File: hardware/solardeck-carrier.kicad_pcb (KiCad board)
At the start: 6 copper layers, 222 x 160 mm, 34 parts, among them J1 DF40C-100DS-0.4V, J2 DF40C-100DS-0.4V, SW1 JS102011SAQN, U1 BQ25895RTWR, U10 W25Q128JVS, U11 DS3231MZ+, U14 TMUX1575YCJR, U15 SN74LVC1G08DBVR, U16 VL805-Q6, U18 ST4SIM-200M, U19 TPS22918DBVR, U2 TPS62840DLYR, U20 INA3221AIRGVR, U21 BQ27441-G1A, U22 TPS2051BDBVR, U23 BMA400, U24 BMP390, U25 TMP112AIDRLR, U26 TUSB320RWBR, U27 TXU0104PWR, U28 MAX98357A, U3 TPS61088RHLR, U4 TPS63020DSJR, U5 BQ25504RGTR, U8 RP2350B, U9 APS6404L-3SQR-SN

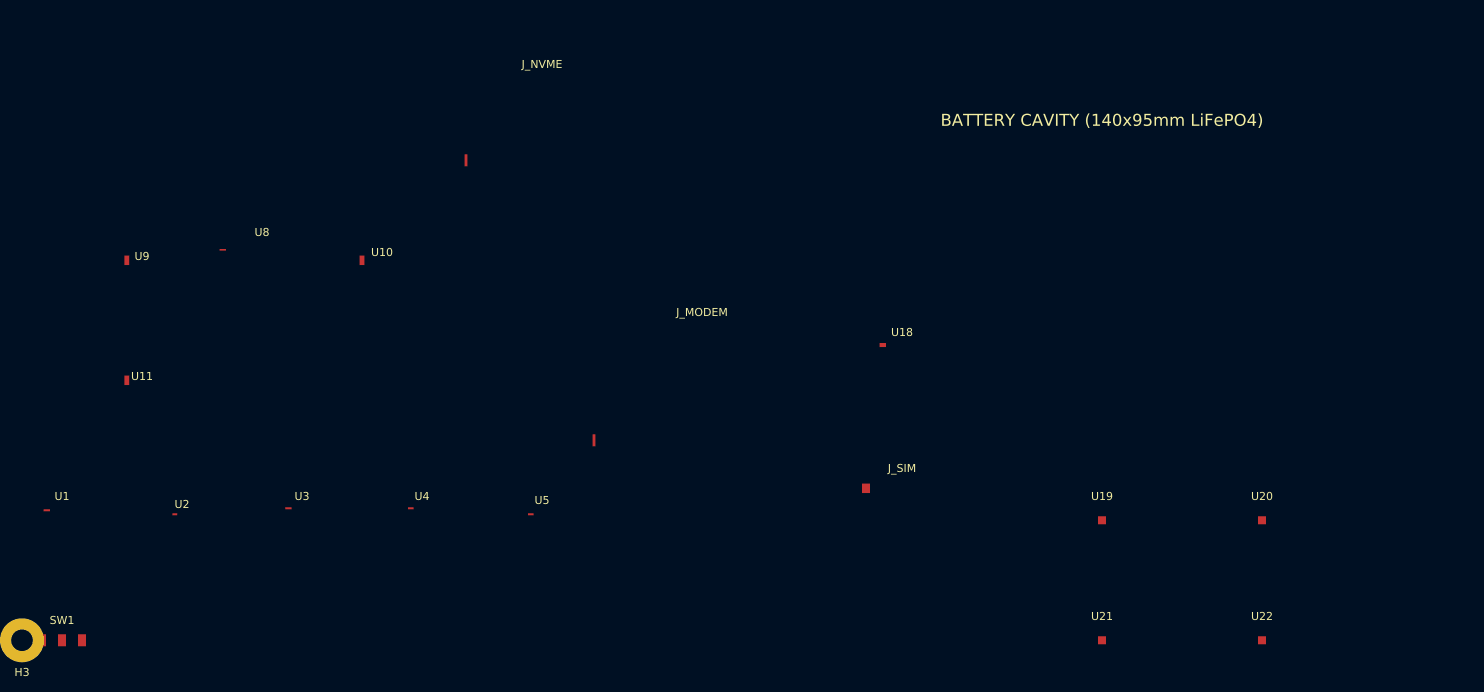
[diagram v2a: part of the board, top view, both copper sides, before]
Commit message: schematic: capture 10 more BOM line items (30/62 -> 40/62) with real LCSC numbers
Batch 2: STUSB4500QTR (PD sink), BQ29700DSET (battery PCM), LM66100DCKR (VBUS
OR-ing), PN5321A3HN (NFC + crypto signer), TPD4E05U06 (ESD TVS), dual
SPH0645LM4H-B (MEMS beamforming pair at 65mm), E22-900M22S (LoRa), PCM5102APWR
(headphone DAC), DRV2605LDGST (haptic).

Footprints datasheet-anchored, incl. corrections the searches caught (TPD4E05
is USON-10 not SOT-23-6, LM66100 is SC-70-6, PCM5102A is TSSOP-20, DRV2605L is
VSSOP-10). capture_schematic_parts.py now also emits kicad_pcb footprint blocks
(reference-grade single pad per U5/U14 convention) and is fully idempotent.
Phase 11 guard extended: live prose restatements must match the netlist.

spec_values baseline 30 -> 40; README/HANDOFF prose normalized; STATUS regenerated.

Co-Authored-By: DeepSeek V4-Flash 0731 <noreply@anthropic.com>
Harness: pi (openrouter/deepseek/deepseek-v4-flash-0731, session 01a15a7c)
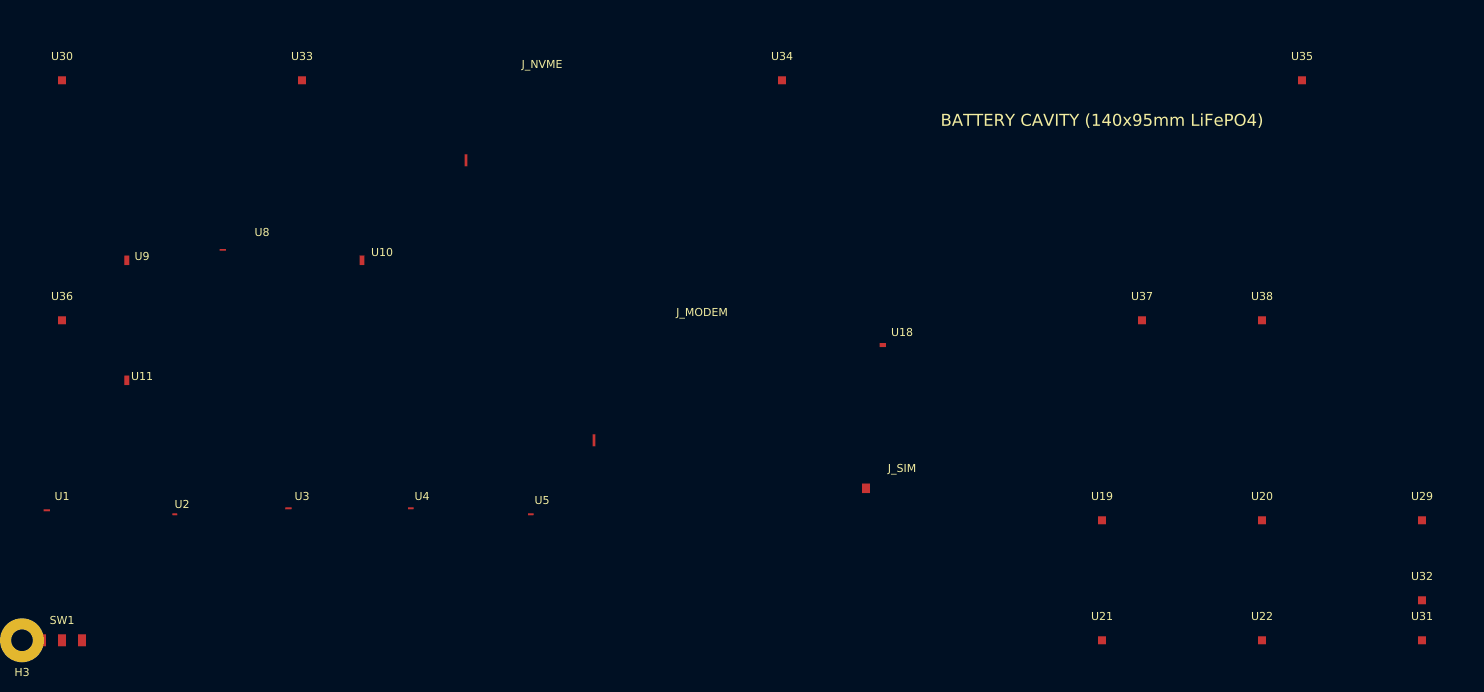
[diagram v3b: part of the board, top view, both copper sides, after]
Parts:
- added U29: STUSB4500QTR, Package_DFN_QFN:VQFN-24-1EP_4x4mm_P0.5mm, F.Cu at (190.0, 135.0)
- added U30: PN5321A3HN, Package_DFN_QFN:HVQFN-40_6x6mm_P0.5mm, F.Cu at (20.0, 80.0)
- added U31: BQ29700DSET, Package_DFN_QFN:WSON-6_1.5x1.5mm_P0.5mm, F.Cu at (190.0, 150.0)
- added U32: LM66100DCKR, Package_TO_SOT_SMD:SC-70-6, F.Cu at (190.0, 145.0)
- added U33: TPD4E05U06, Package_DFN_QFN:USON-10_2.5x1mm_P0.5mm, F.Cu at (50.0, 80.0)
- added U34: SPH0645LM4H-B, Package_LGA:MIC-SMD-6P_3.5x2.65mm_P0.9mm, F.Cu at (110.0, 80.0)
- added U35: SPH0645LM4H-B, Package_LGA:MIC-SMD-6P_3.5x2.65mm_P0.9mm, F.Cu at (175.0, 80.0)
- added U36: E22-900M22S, Module_EByte:E22-900M22S_20x14mm, F.Cu at (20.0, 110.0)
- added U37: PCM5102APWR, Package_SO:TSSOP-20_6.5x4.4mm_P0.65mm, F.Cu at (155.0, 110.0)
- added U38: DRV2605LDGST, Package_TO_SOT_SMD:VSSOP-10_3x4.9mm_P0.5mm, F.Cu at (170.0, 110.0)
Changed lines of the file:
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@@
     (pad "1" smd rect (at 0 0) (size 1.0 1.0) (layers "F.Cu" "F.Paste" "F.Mask"))
   )
-)
+  (footprint "Package_DFN_QFN:VQFN-24-1EP_4x4mm_P0.5mm" (layer "F.Cu")
+    (at 190.0 135.0)
+    (fp_text reference "U29" (at 0 -3.0) (layer "F.SilkS") (effects (font (size 1 1) (thickness 0.15))))
+    (fp_text value "STUSB4500QTR" (at 0 3.0) (layer "F.Fab") (effects (font (size 1 1) (thickness 0.15))))
+    (pad "1" smd rect (at 0 0) (size 1.0 1.0) (layers "F.Cu" "F.Paste" "F.Mask"))
+  )
+  (footprint "Package_DFN_QFN:WSON-6_1.5x1.5mm_P0.5mm" (layer "F.Cu")
+    (at 190.0 150.0)
+    (fp_text reference "U31" (at 0 -3.0) (layer "F.SilkS") (effects (font (size 1 1) (thickness 0.15))))
+    (fp_text value "BQ29700DSET" (at 0 3.0) (layer "F.Fab") (effects (font (size 1 1) (thickness 0.15))))
+    (pad "1" smd rect (at 0 0) (size 1.0 1.0) (layers "F.Cu" "F.Paste" "F.Mask"))
+  )
+  (footprint "Package_TO_SOT_SMD:SC-70-6" (layer "F.Cu")
+    (at 190.0 145.0)
+    (fp_text reference "U32" (at 0 -3.0) (layer "F.SilkS") (effects (font (size 1 1) (thickness 0.15))))
+    (fp_text value "LM66100DCKR" (at 0 3.0) (layer "F.Fab") (effects (font (size 1 1) (thickness 0.15))))
+    (pad "1" smd rect (at 0 0) (size 1.0 1.0) (layers "F.Cu" "F.Paste" "F.Mask"))
+  )
+  (footprint "Package_DFN_QFN:HVQFN-40_6x6mm_P0.5mm" (layer "F.Cu")
+    (at 20.0 80.0)
+    (fp_text reference "U30" (at 0 -3.0) (layer "F.SilkS") (effects (font (size 1 1) (thickness 0.15))))
+    (fp_text value "PN5321A3HN" (at 0 3.0) (layer "F.Fab") (effects (font (size 1 1) (thickness 0.15))))
+    (pad "1" smd rect (at 0 0) (size 1.0 1.0) (layers "F.Cu" "F.Paste" "F.Mask"))
+  )
+  (footprint "Package_DFN_QFN:USON-10_2.5x1mm_P0.5mm" (layer "F.Cu")
+    (at 50.0 80.0)
+    (fp_text reference "U33" (at 0 -3.0) (layer "F.SilkS") (effects (font (size 1 1) (thickness 0.15))))
+    (fp_text value "TPD4E05U06" (at 0 3.0) (layer "F.Fab") (effects (font (size 1 1) (thickness 0.15))))
+    (pad "1" smd rect (at 0 0) (size 1.0 1.0) (layers "F.Cu" "F.Paste" "F.Mask"))
+  )
+  (footprint "Package_LGA:MIC-SMD-6P_3.5x2.65mm_P0.9mm" (layer "F.Cu")
+    (at 110.0 80.0)
+    (fp_text reference "U34" (at 0 -3.0) (layer "F.SilkS") (effects (font (size 1 1) (thickness 0.15))))
+    (fp_text value "SPH0645LM4H-B" (at 0 3.0) (layer "F.Fab") (effects (font (size 1 1) (thickness 0.15))))
+    (pad "1" smd rect (at 0 0) (size 1.0 1.0) (layers "F.Cu" "F.Paste" "F.Mask"))
+  )
+  (footprint "Package_LGA:MIC-SMD-6P_3.5x2.65mm_P0.9mm" (layer "F.Cu")
+    (at 175.0 80.0)
+    (fp_text reference "U35" (at 0 -3.0) (layer "F.SilkS") (effects (font (size 1 1) (thickness 0.15))))
+    (fp_text value "SPH0645LM4H-B" (at 0 3.0) (layer "F.Fab") (effects (font (size 1 1) (thickness 0.15))))
+    (pad "1" smd rect (at 0 0) (size 1.0 1.0) (layers "F.Cu" "F.Paste" "F.Mask"))
+  )
+  (footprint "Module_EByte:E22-900M22S_20x14mm" (layer "F.Cu")
+    (at 20.0 110.0)
+    (fp_text reference "U36" (at 0 -3.0) (layer "F.SilkS") (effects (font (size 1 1) (thickness 0.15))))
+    (fp_text value "E22-900M22S" (at 0 3.0) (layer "F.Fab") (effects (font (size 1 1) (thickness 0.15))))
+    (pad "1" smd rect (at 0 0) (size 1.0 1.0) (layers "F.Cu" "F.Paste" "F.Mask"))
+  )
+  (footprint "Package_SO:TSSOP-20_6.5x4.4mm_P0.65mm" (layer "F.Cu")
+    (at 155.0 110.0)
+    (fp_text reference "U37" (at 0 -3.0) (layer "F.SilkS") (effects (font (size 1 1) (thickness 0.15))))
+    (fp_text value "PCM5102APWR" (at 0 3.0) (layer "F.Fab") (effects (font (size 1 1) (thickness 0.15))))
+    (pad "1" smd rect (at 0 0) (size 1.0 1.0) (layers "F.Cu" "F.Paste" "F.Mask"))
+  )
+  (footprint "Package_TO_SOT_SMD:VSSOP-10_3x4.9mm_P0.5mm" (layer "F.Cu")
+    (at 170.0 110.0)
+    (fp_text reference "U38" (at 0 -3.0) (layer "F.SilkS") (effects (font (size 1 1) (thickness 0.15))))
+    (fp_text value "DRV2605LDGST" (at 0 3.0) (layer "F.Fab") (effects (font (size 1 1) (thickness 0.15))))
+    (pad "1" smd rect (at 0 0) (size 1.0 1.0) (layers "F.Cu" "F.Paste" "F.Mask"))
+  ))
